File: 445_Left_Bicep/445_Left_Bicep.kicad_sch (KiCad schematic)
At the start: 7 parts, among them J1 69167-114HLF, J2 SM02B-SRSS-TB_LF__SN_, J3 87583-2010RPLF, U1 ESP32-S3-WROOM-1-N16R8, U2 LSM6DSMTR, U3 LP2950CZ-3.3_LFT3

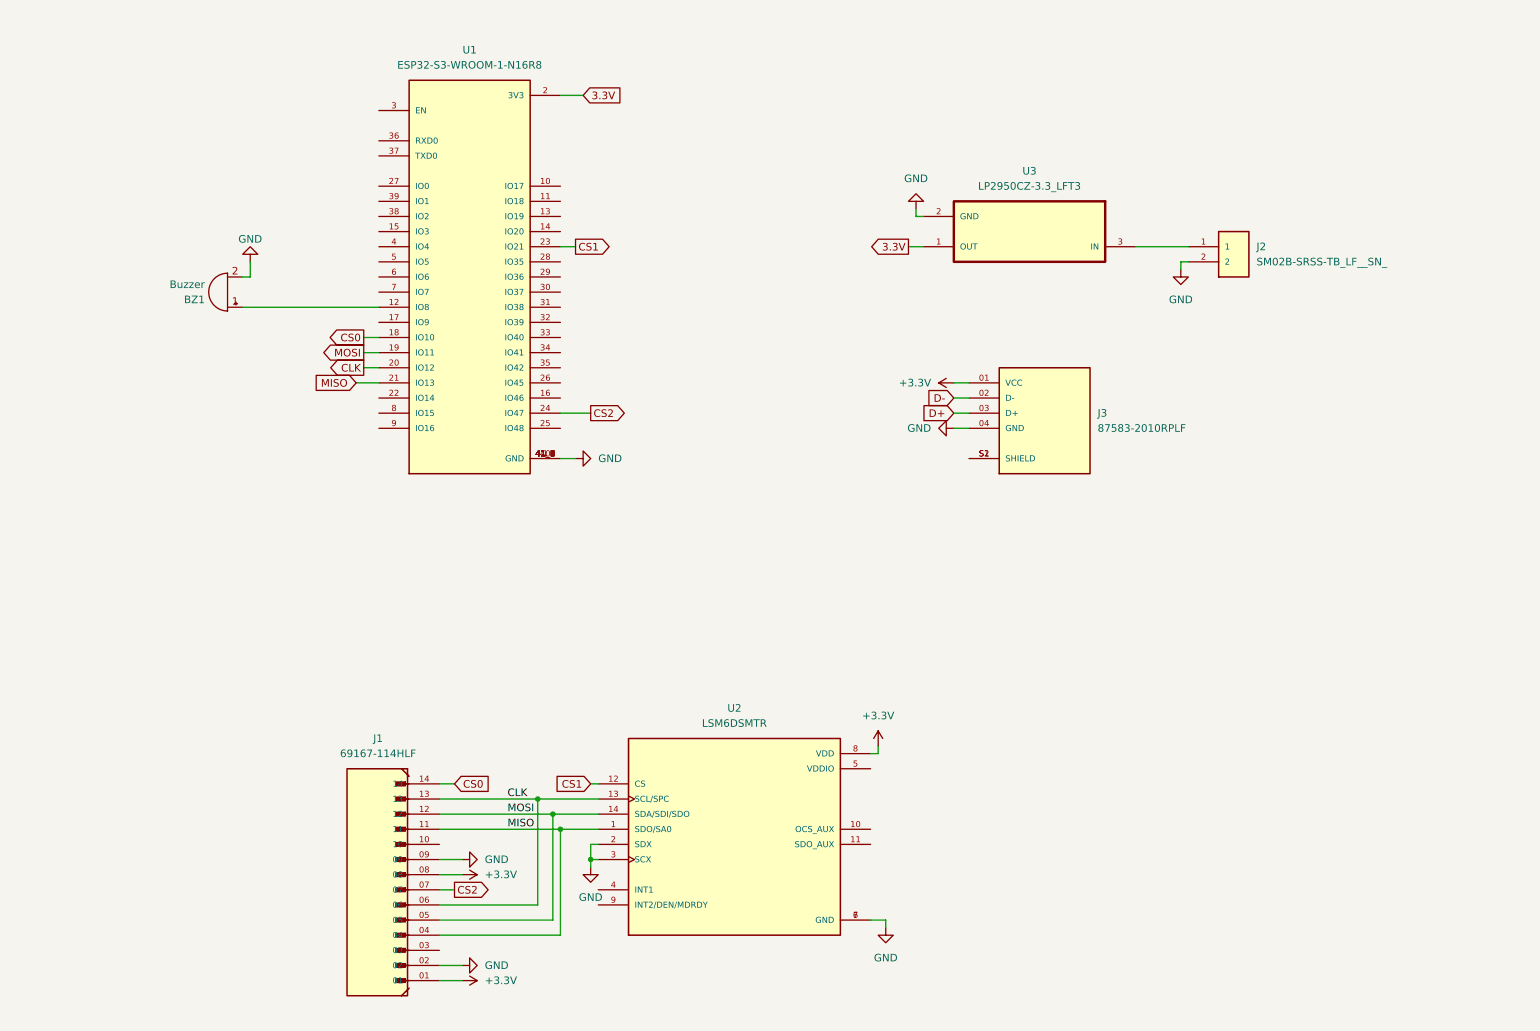
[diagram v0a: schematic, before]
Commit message: enable signal and analog switches
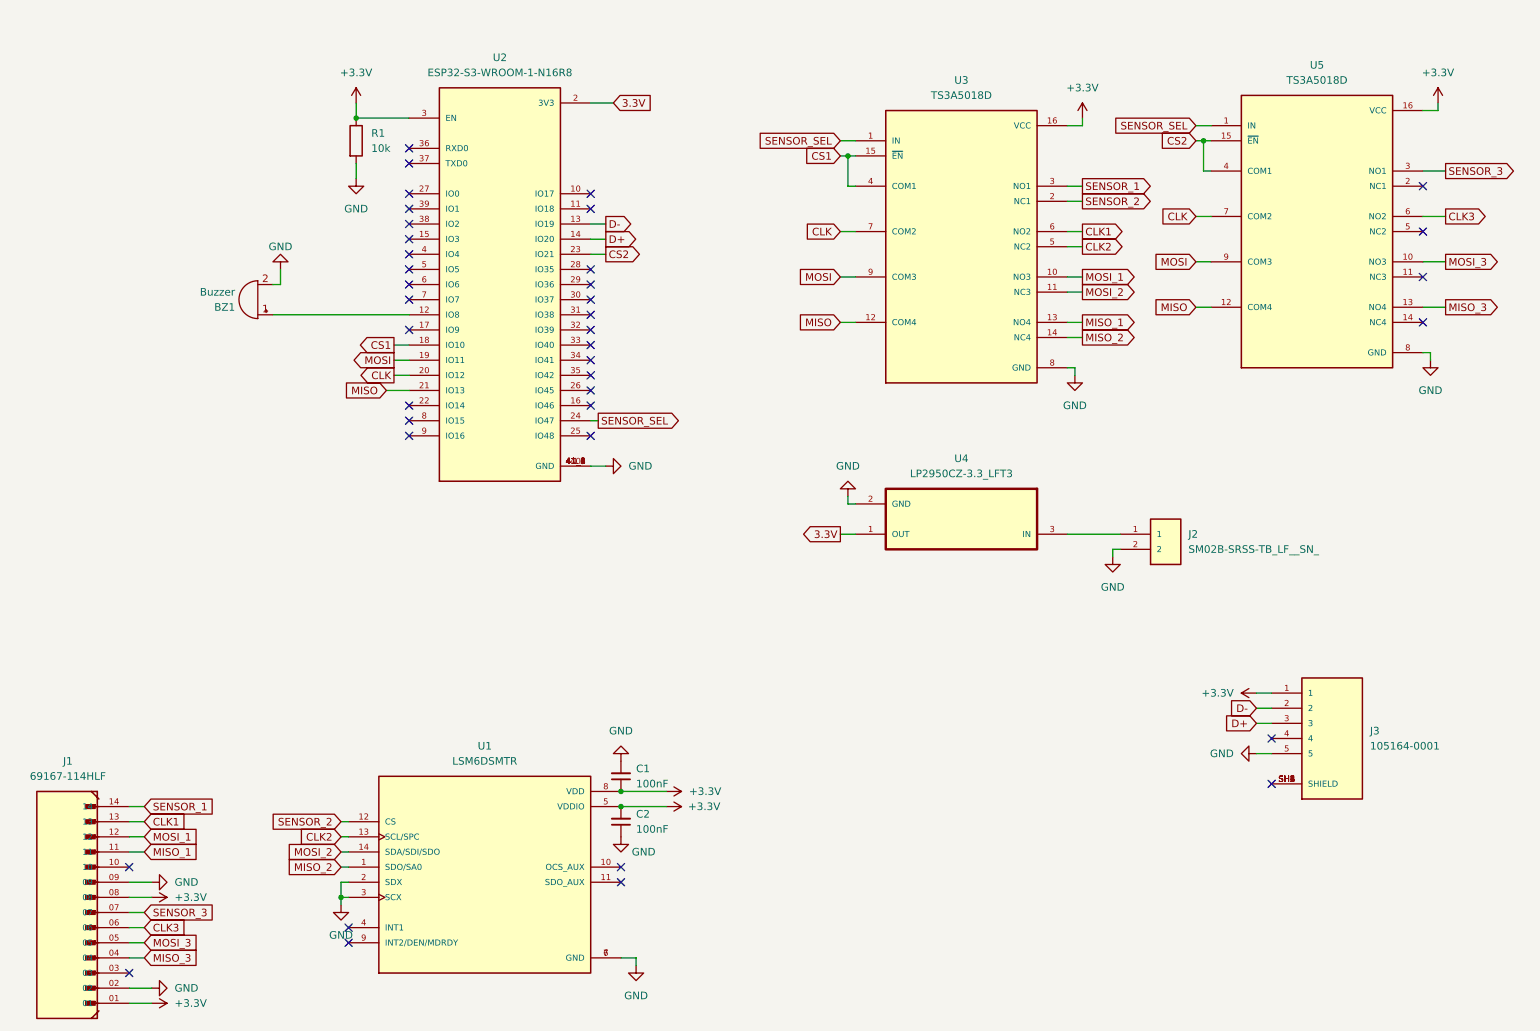
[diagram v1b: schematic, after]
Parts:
- removed J3: 87583-2010RPLF, 87583-2010RPLF:AMPHENOL_87583-2010RPLF, symbol 87583-2010RPLF:87583-2010RPLF
- removed U1: ESP32-S3-WROOM-1-N16R8, ESP32-S3-WROOM-1-N16R8:XCVR_ESP32-S3-WROOM-1-N16R8, symbol ESP32-S3-WROOM-1-N16R8:ESP32-S3-WROOM-1-N16R8
- removed U2: LSM6DSMTR, LSM6DSMTR (1):PQFN50P300X250X86-14N, symbol LSM6DSMTR:LSM6DSMTR
- removed U3: LP2950CZ-3.3_LFT3, LP2950CZ-3.3_LFT3:TO92127P521H735-3, symbol LP2950CZ-3.3_LFT3:LP2950CZ-3.3_LFT3
- added C1, C2: 100nF, symbol Device:C_Small
- added J3: 105164-0001, 105164-0001:MOLEX_105164-0001, symbol 105164-0001:105164-0001
- added R1: 10k, symbol Device:R
- added U1: LSM6DSMTR, LSM6DSMTR (1):PQFN50P300X250X86-14N, symbol LSM6DSMTR:LSM6DSMTR
- added U2: ESP32-S3-WROOM-1-N16R8, ESP32-S3-WROOM-1-N16R8:XCVR_ESP32-S3-WROOM-1-N16R8, symbol ESP32-S3-WROOM-1-N16R8:ESP32-S3-WROOM-1-N16R8
- added U3, U5: TS3A5018D, TS3A5018D:SOIC127P600X175-16N, symbol TS3A5018D:TS3A5018D
- added U4: LP2950CZ-3.3_LFT3, LP2950CZ-3.3_LFT3:TO92127P521H735-3, symbol LP2950CZ-3.3_LFT3:LP2950CZ-3.3_LFT3
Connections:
- net +3.3V: now also C1.1, C2.2, J3.1, R1.1, U1.5 (VDDIO), U1.8 (VDD), U2.3 (EN), U3.16 (VCC), U5.16 (VCC)
- net 3.3V: now also U2.2 (3V3), U4.1 (OUT)
- net CLK: now also U2.20 (IO12), U3.7 (COM2), U5.7 (COM2); no longer J1.06, J1.13
- net CS1: now also U2.18 (IO10), U3.15 (~{EN}), U3.4 (COM1)
- net CS2: now also U2.23 (IO21), U5.15 (~{EN}), U5.4 (COM1); no longer J1.07
- net D+: now also J3.3, U2.14 (IO20)
- net D-: now also J3.2, U2.13 (IO19)
- net GND: now also C1.2, C2.1, J3.5, R1.2, U1.2 (SDX), U1.3 (SCX), U1.6 (GND), U1.7 (GND), U2.1 (GND), U2.40 (GND), U2.41_1 (GND), U2.41_2 (GND), U2.41_3 (GND), U2.41_4 (GND), U2.41_5 (GND), U2.41_6 (GND), U2.41_7 (GND), U2.41_8 (GND), U2.41_9 (GND), U3.8 (GND), U4.2 (GND), U5.8 (GND)
- net MISO: now also U2.21 (IO13), U3.12 (COM4), U5.12 (COM4); no longer J1.04, J1.11
- net MOSI: now also U2.19 (IO11), U3.9 (COM3), U5.9 (COM3); no longer J1.05, J1.12
- net at J2.1: now also U4.3 (IN)
- net at BZ1.1 (+): now also U2.12 (IO8)
- net CS0 renamed SENSOR_1
- net SENSOR_1: now also U3.3 (NO1)
- new net: J3.SH1 (SHIELD), J3.SH2 (SHIELD), J3.SH3 (SHIELD), J3.SH4 (SHIELD), J3.SH5 (SHIELD), J3.SH6 (SHIELD)
- new net CLK1: J1.13, U3.6 (NO2)
- new net CLK2: U1.13 (SCL/SPC), U3.5 (NC2)
- new net CLK3: J1.06, U5.6 (NO2)
- new net MISO_1: J1.11, U3.13 (NO4)
- new net MISO_2: U1.1 (SDO/SA0), U3.14 (NC4)
- new net MISO_3: J1.04, U5.13 (NO4)
- new net MOSI_1: J1.12, U3.10 (NO3)
- new net MOSI_2: U1.14 (SDA/SDI/SDO), U3.11 (NC3)
- new net MOSI_3: J1.05, U5.10 (NO3)
- new net SENSOR_2: U1.12 (CS), U3.2 (NC1)
- new net SENSOR_3: J1.07, U5.3 (NO1)
- new net SENSOR_SEL: U2.24 (IO47), U3.1 (IN), U5.1 (IN)
- no-connect marks 0 -> 39

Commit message: replace bicep connector and add int1 connections
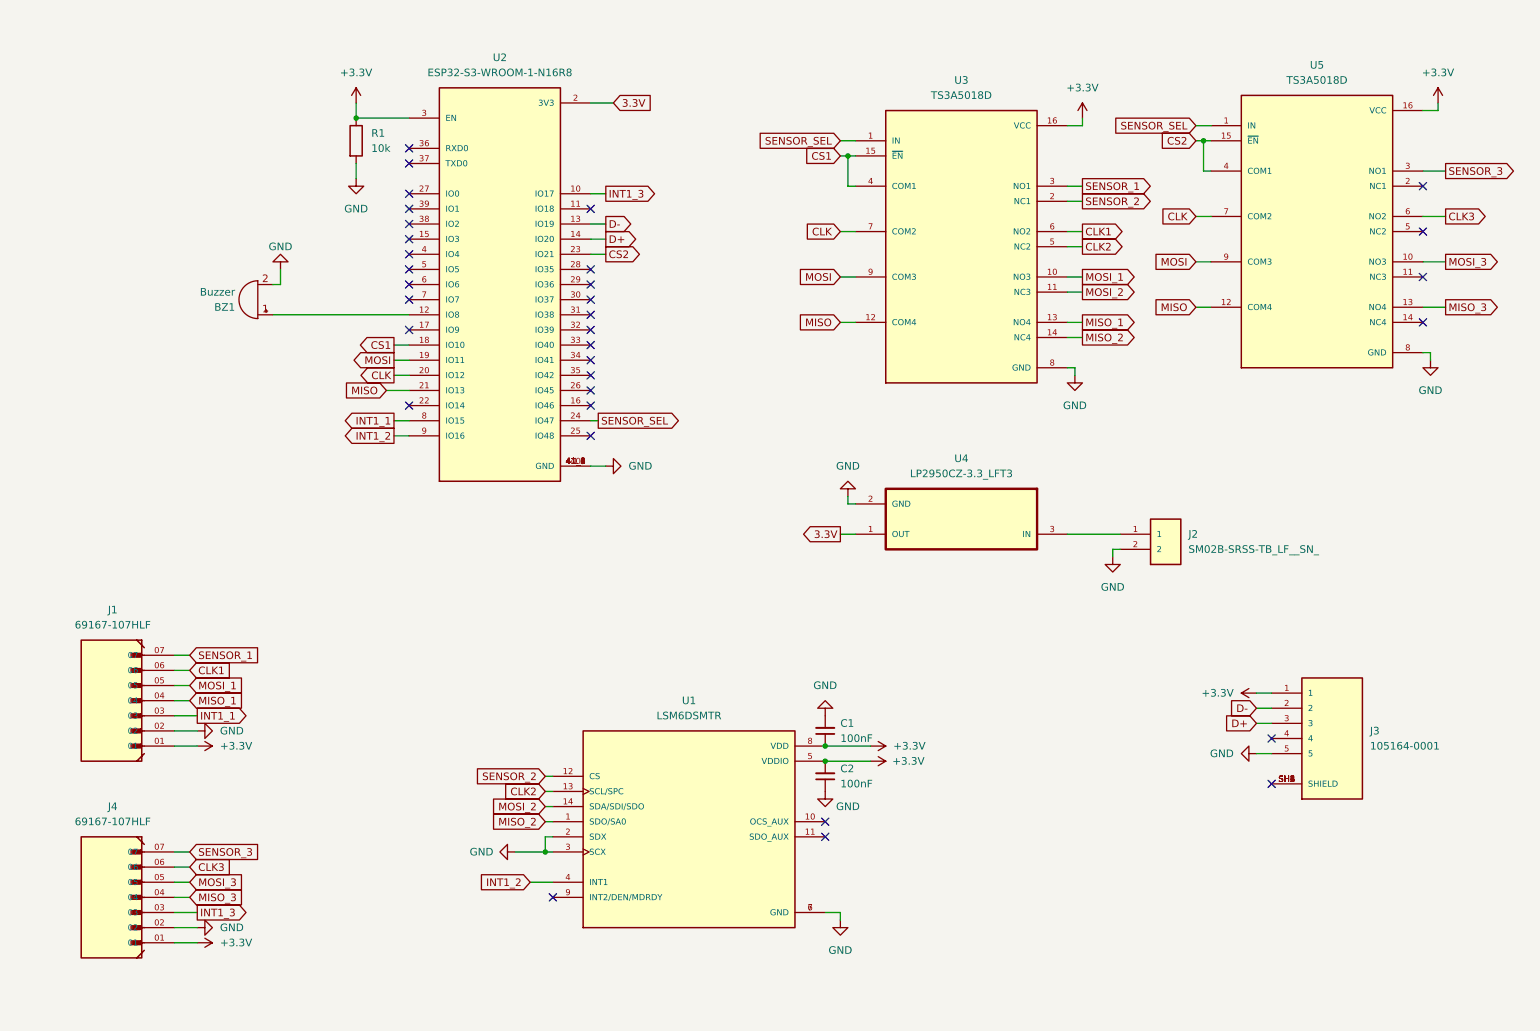
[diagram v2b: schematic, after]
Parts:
- removed J1: 69167-114HLF, 69167-114HLF:AMPHENOL_69167-114HLF, symbol 69167-114HLF:69167-114HLF
- added J1, J4: 69167-107HLF, 69167-107HLF:AMPHENOL_69167-107HLF, symbol 69167-107HLF:69167-107HLF
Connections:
- net +3.3V: now also J1.01, J4.01
- net CLK1: now also J1.06
- net CLK3: now also J4.06
- net GND: now also J1.02, J4.02
- net MISO_1: now also J1.04
- net MISO_3: now also J4.04
- net MOSI_1: now also J1.05
- net MOSI_3: now also J4.05
- net SENSOR_1: now also J1.07
- net SENSOR_3: now also J4.07
- net INT1_2: now reaches U1.4 (INT1)
- net INT1_2: now also U2.9 (IO16)
- net INT1_3: now reaches U2.10 (IO17)
- net INT1_3: now also J4.03
- net INT1_1: now reaches U2.8 (IO15)
- net INT1_1: now also J1.03
- no-connect marks 39 -> 33
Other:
- moved on the sheet: C1, C2, U1

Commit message: Layout First Draft
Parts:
- removed J3: 105164-0001, 105164-0001:MOLEX_105164-0001, symbol 105164-0001:105164-0001
- added H1, H2, H3, H4: MountingHole, MountingHole:MountingHole_2mm, symbol Mechanical:MountingHole
- added J3: 87583-2010RPLF, 87583-2010RPLF:AMPHENOL_87583-2010RPLF, symbol 87583-2010RPLF:87583-2010RPLF
- C1, C2: footprint (none) -> CL21F104ZAANNNC:CAPC2012X135N
- R1: footprint (none) -> RMCF0805JG10K0:RESC2012X65N
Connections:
- net 3.3V is gone; now on net +3.3V: U2.2 (3V3), U4.1 (OUT)
- net +3.3V: now also J3.01 (VCC)
- net D+: now also J3.03 (D+)
- net D-: now also J3.02 (D-)
- net GND: now also J3.04 (GND)
- net MISO: now also U2.19 (IO11); no longer U2.21 (IO13)
- net MOSI: now also U2.21 (IO13); no longer U2.19 (IO11)
- net 3.7V: now reaches J2.1, U4.3 (IN)
- new net: J3.S1 (SHIELD), J3.S2 (SHIELD)
- no-connect marks 33 -> 32
